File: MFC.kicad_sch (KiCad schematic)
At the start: 25 parts, among them J1 DB15_Female_MountingHoles, J10 Conn_01x01_Male, J11 Conn_01x01_Male, J12 Conn_01x01_Male, J2 Conn_01x04_Male, J4 647676-3, J5 Conn_01x01_Male, J6 Conn_01x01_Male

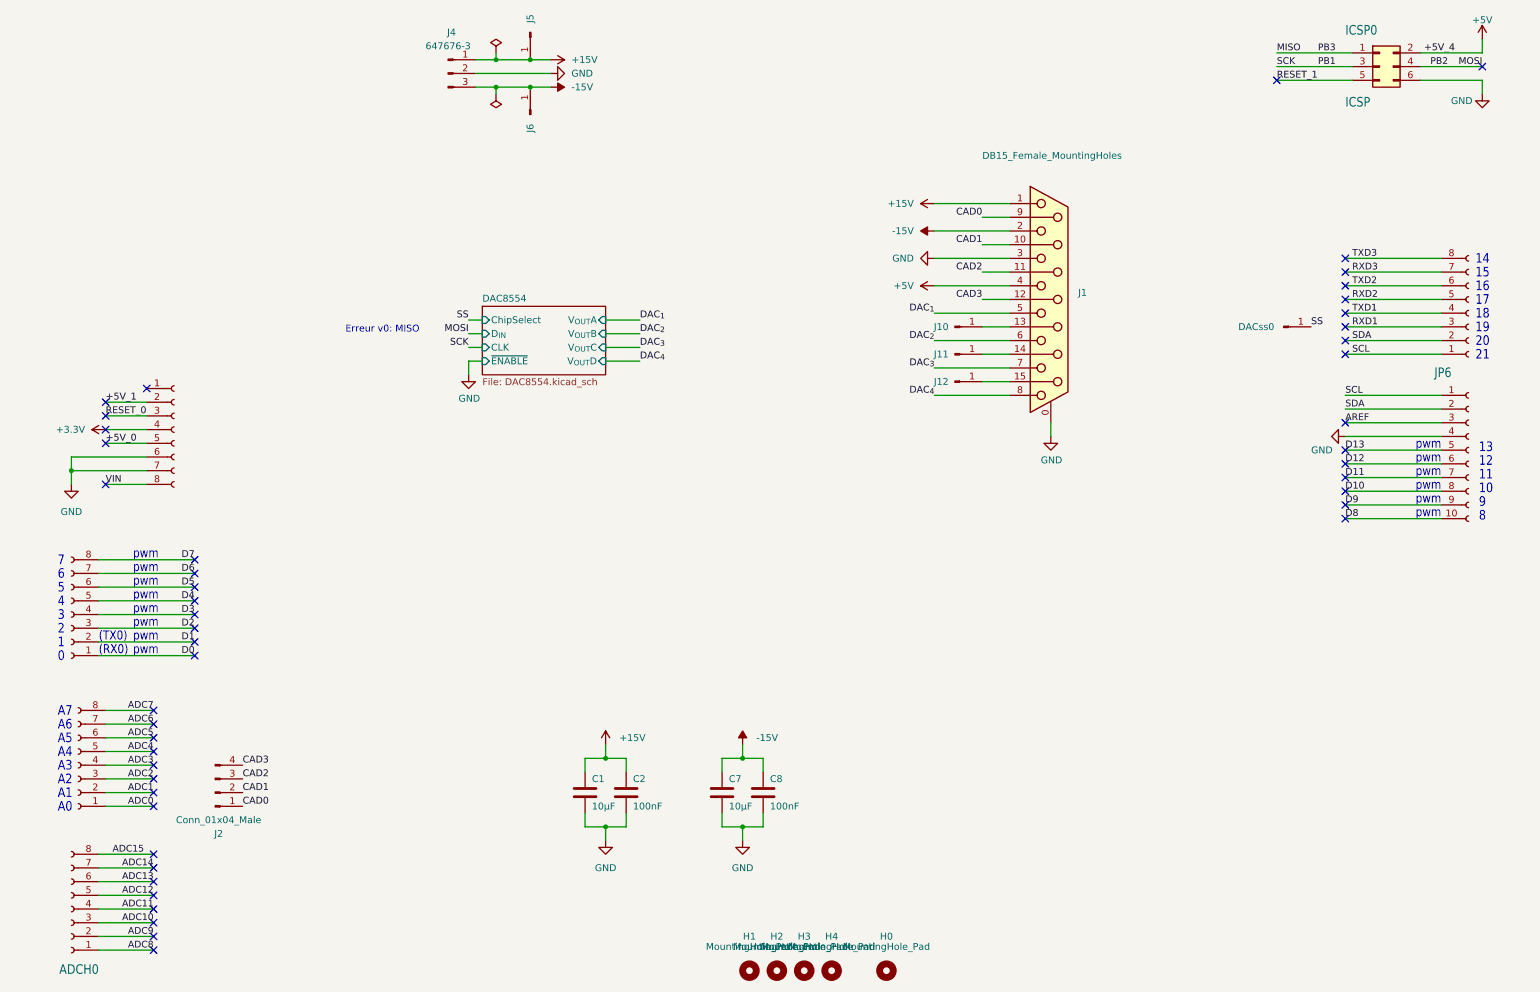
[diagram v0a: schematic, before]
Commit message: Update to KiCad 7
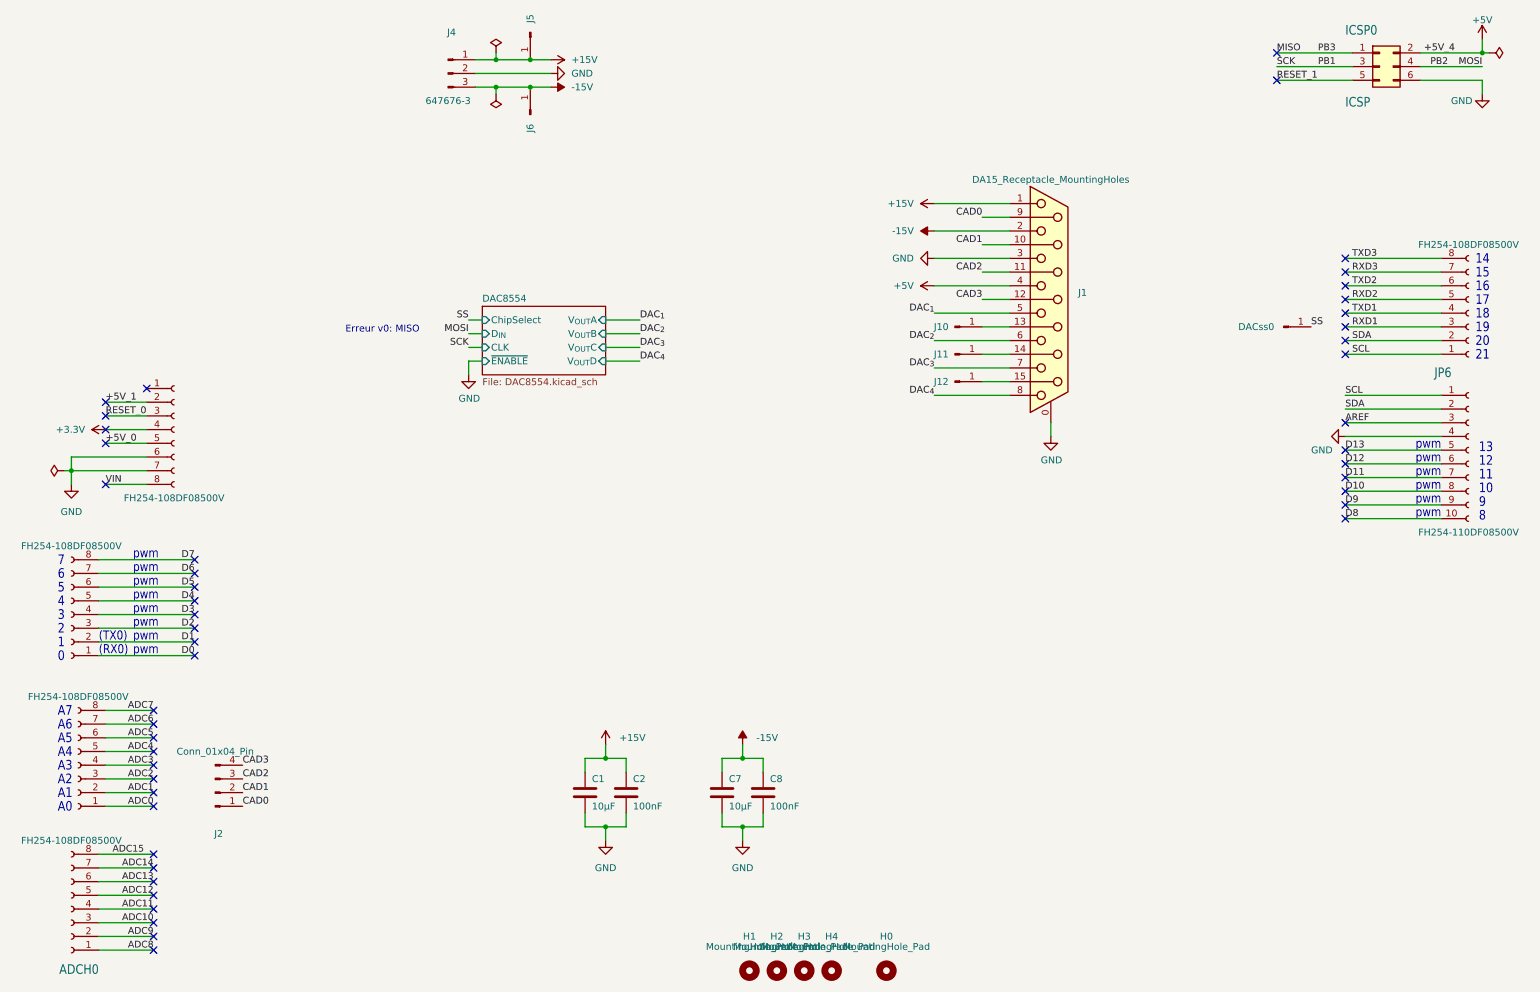
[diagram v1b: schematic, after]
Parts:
- ADCH0, ADCL0, COMMUNICATION0, POWER0, PWML0: symbol Connector:Conn_01x08_Female -> Connector:Conn_01x08_Socket
- DACss0, J10, J11, J12, J5, J6: value Conn_01x01_Male -> Conn_01x01_Pin; symbol Connector:Conn_01x01_Male -> Connector:Conn_01x01_Pin
- J1: value DB15_Female_MountingHoles -> DA15_Receptacle_MountingHoles; symbol Connector:DB15_Female_MountingHoles -> Connector:DA15_Receptacle_MountingHoles
- J2: value Conn_01x04_Male -> Conn_01x04_Pin; symbol Connector:Conn_01x04_Male -> Connector:Conn_01x04_Pin
- J4: symbol Connector:Conn_01x03_Male -> Connector:Conn_01x03_Pin
- JP6: symbol Connector:Conn_01x10_Female -> Connector:Conn_01x10_Socket

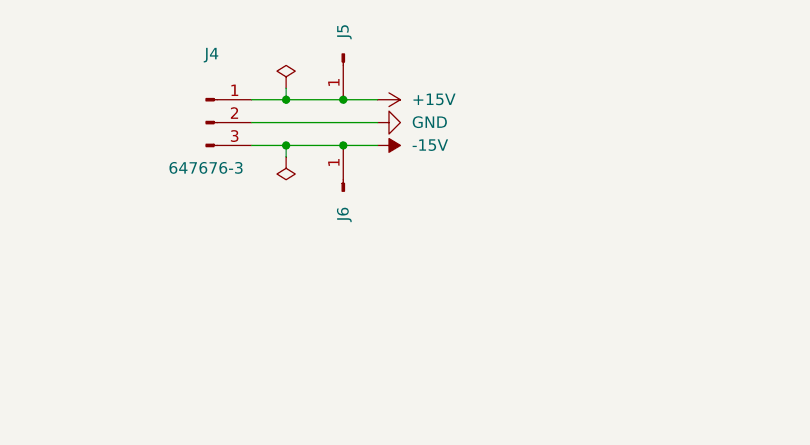
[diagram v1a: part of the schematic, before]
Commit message: Changed transversal power connector
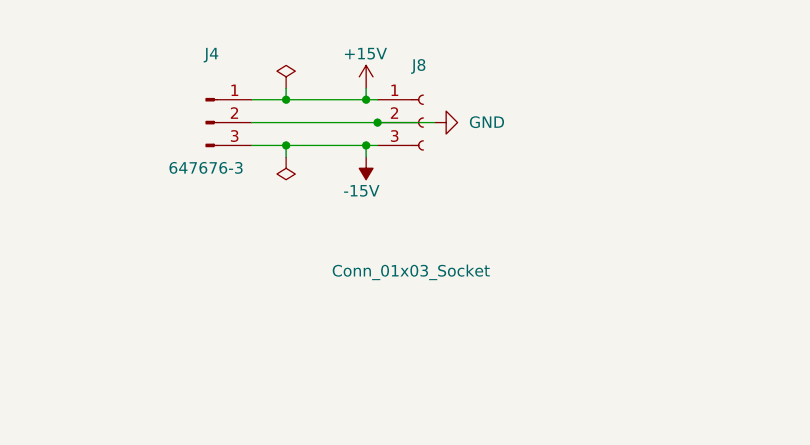
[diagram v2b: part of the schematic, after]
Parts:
- removed J5, J6: Conn_01x01_Pin, Connector_PinHeader_2.54mm:PinHeader_1x01_P2.54mm_Vertical, symbol Connector:Conn_01x01_Pin
- added J8: Conn_01x03_Socket, Connector_PinSocket_2.54mm:PinSocket_1x03_P2.54mm_Vertical, symbol Connector:Conn_01x03_Socket
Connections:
- net +15V: now also J8.1 (Pin_1)
- net -15V: now also J8.3 (Pin_3)
- net GND: now also J8.2 (Pin_2)

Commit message: Added MAX232 Optimised DAC8554 Routing
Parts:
- removed J10, J11: Conn_01x01_Pin, Connector_PinHeader_2.54mm:PinHeader_1x01_P2.54mm_Vertical, symbol Connector:Conn_01x01_Pin
- added J5, J6: Conn_01x03_Pin, Connector_PinHeader_2.54mm:PinHeader_1x03_P2.54mm_Vertical, symbol Connector:Conn_01x03_Pin
- added R1, R3: 0, Resistor_SMD:R_0603_1608Metric_Pad0.98x0.95mm_HandSolder, symbol Device:R
- added R2, R4: R, Resistor_SMD:R_0603_1608Metric_Pad0.98x0.95mm_HandSolder, symbol Device:R
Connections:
- net GND: now also R2.2, R4.2
- net RXD2: now also J6.1 (Pin_1)
- net TXD2: now also J5.1 (Pin_1)
- net Serial_MISO: now reaches J1.14 (P14)
- net Serial_MISO: now also R3.2, R4.1
- net Serial_MOSI: now reaches J1.13 (P13)
- net Serial_MOSI: now also R1.2, R2.1
- new net: J6.2 (Pin_2), R3.1
- new net: J5.2 (Pin_2), R1.1
- new net RS232_MISO: J6.3 (Pin_3)
- new net RS232_MOSI: J5.3 (Pin_3)
- no-connect marks 47 -> 45
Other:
- added sheet MAX232 (MAX232.kicad_sch)
- moved on the sheet: C1, C2, C7, C8

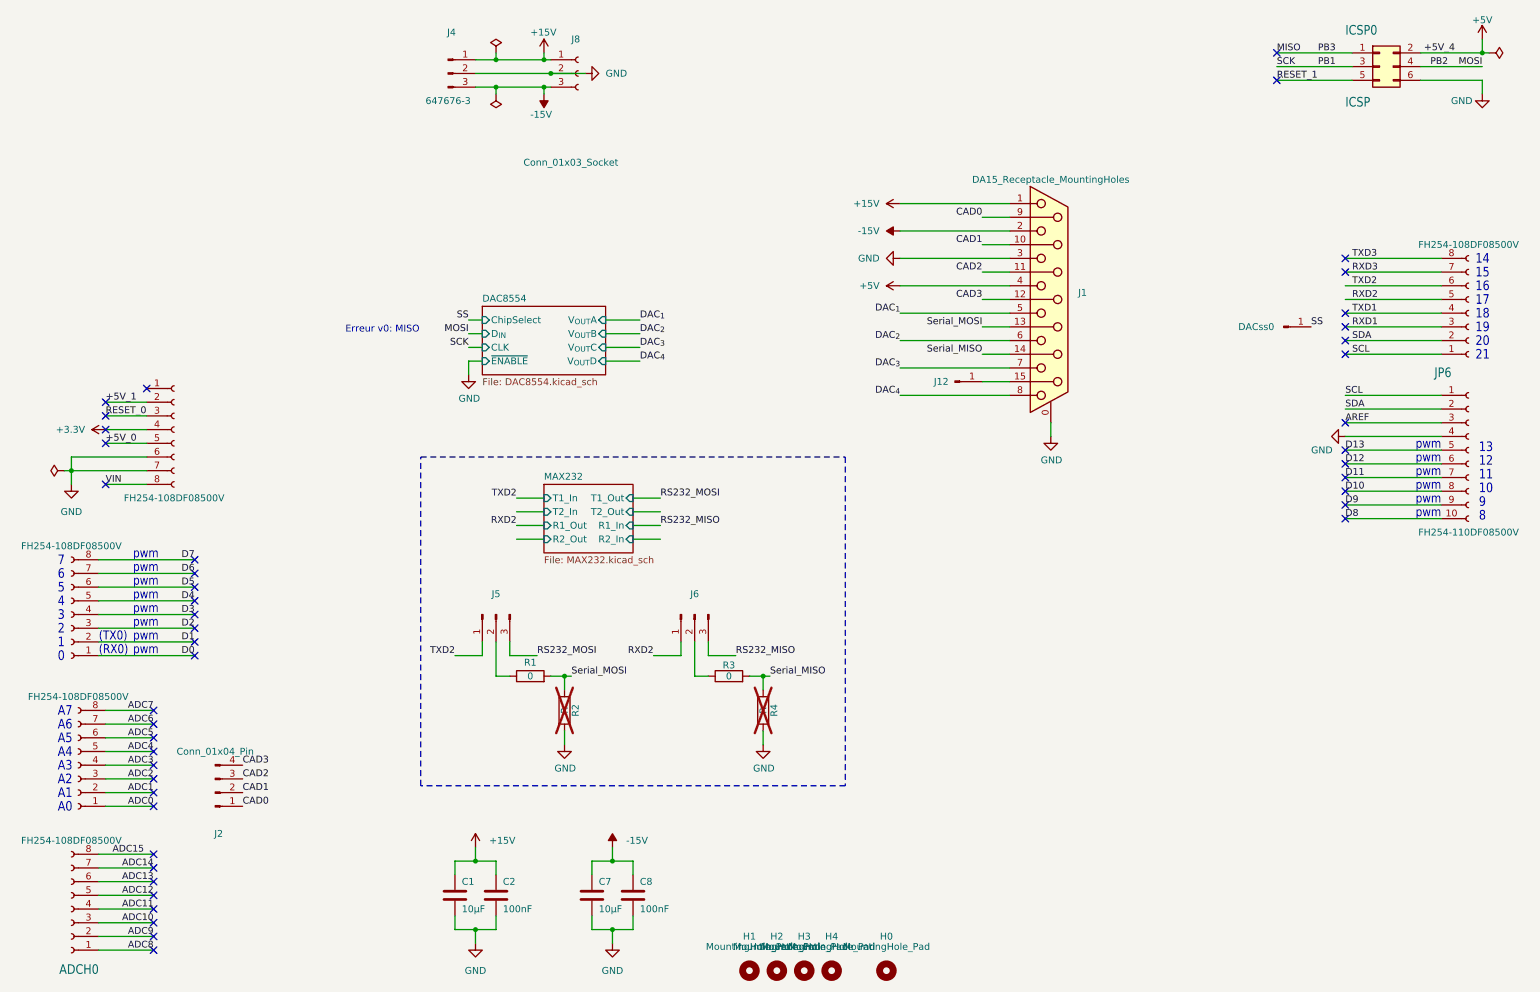
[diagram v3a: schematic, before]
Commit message: Added choice for serial com
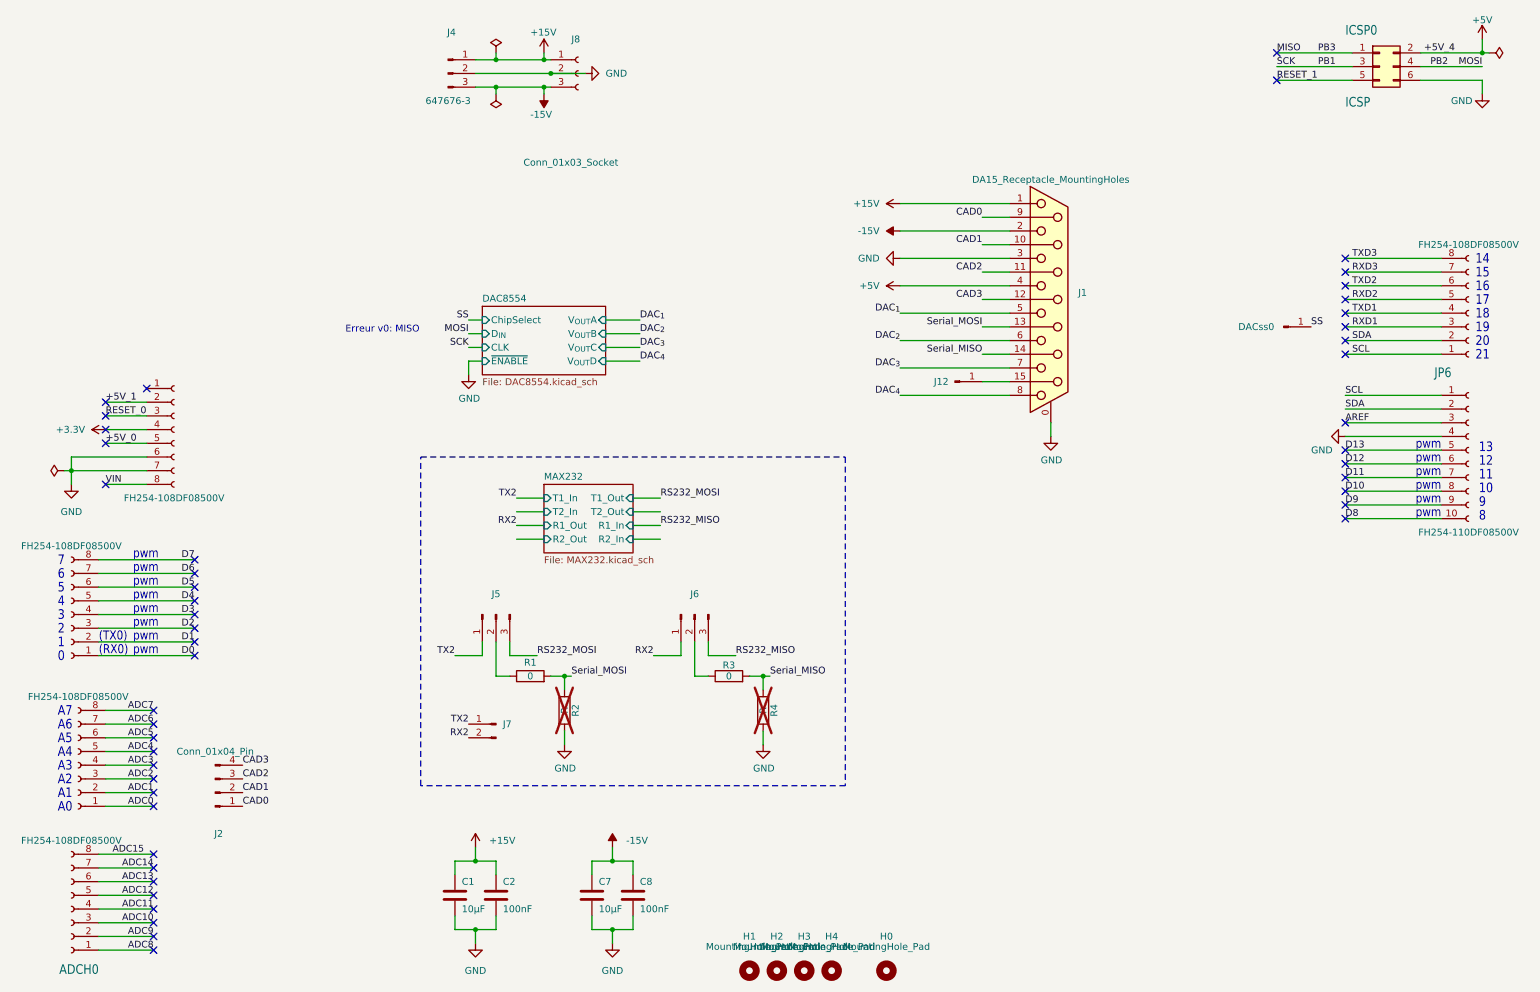
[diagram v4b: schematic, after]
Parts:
- added J7: Conn_01x02_Pin, Connector_PinHeader_2.54mm:PinHeader_1x02_P2.54mm_Vertical, symbol Connector:Conn_01x02_Pin
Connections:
- net RXD2: no longer J6.1 (Pin_1)
- net TXD2: no longer J5.1 (Pin_1)
- new net RX2: J6.1 (Pin_1), J7.2 (Pin_2)
- new net TX2: J5.1 (Pin_1), J7.1 (Pin_1)
- no-connect marks 45 -> 47
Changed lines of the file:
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@@
   (no_connect (at 31.75 176.53))
   (no_connect (at 22.86 102.87))
+  (no_connect (at 252.73 68.58))
   (no_connect (at 252.73 60.96))
   (no_connect (at 39.37 121.92))
@@
   (no_connect (at 31.75 189.23))
   (no_connect (at 31.75 181.61))
+  (no_connect (at 252.73 66.04))
   (no_connect (at 31.75 152.4))
   (no_connect (at 30.48 85.09))
@@
     (effects (font (size 1.27 1.27)) (justify right bottom))
   )
-  (label "RXD2" (at 124.46 134.62 180) (fields_autoplaced)
+  (label "RX2" (at 124.46 134.62 180) (fields_autoplaced)
     (effects (font (size 1.2446 1.2446)) (justify right bottom))
   )
@@
     (effects (font (size 1.27 1.27)) (justify left bottom))
   )
-  (label "TXD2" (at 99.06 105.41 180) (fields_autoplaced)
+  (label "TX2" (at 99.06 105.41 180) (fields_autoplaced)
     (effects (font (size 1.2446 1.2446)) (justify right bottom))
   )
@@
     (effects (font (size 1.27 1.27)) (justify left bottom))
   )
+  (label "TX2" (at 90.17 147.32 180) (fields_autoplaced)
+    (effects (font (size 1.2446 1.2446)) (justify right bottom))
+  )
   (label "D8" (at 252.73 109.22 0) (fields_autoplaced)
     (effects (font (size 1.27 1.27)) (justify left bottom))
@@
     (effects (font (size 1.2446 1.2446)) (justify left bottom))
   )
-  (label "TXD2" (at 87.63 134.62 180) (fields_autoplaced)
-    (effects (font (size 1.2446 1.2446)) (justify right bottom))
-  )
-  (label "RXD2" (at 99.06 110.49 180) (fields_autoplaced)
+  (label "TX2" (at 87.63 134.62 180) (fields_autoplaced)
+    (effects (font (size 1.2446 1.2446)) (justify right bottom))
+  )
+  (label "RX2" (at 90.17 149.86 180) (fields_autoplaced)
+    (effects (font (size 1.2446 1.2446)) (justify right bottom))
+  )
+  (label "RX2" (at 99.06 110.49 180) (fields_autoplaced)
     (effects (font (size 1.2446 1.2446)) (justify right bottom))
   )
@@
         )
       )
+    )
+  )
+  (symbol (lib_id "Connector:Conn_01x02_Pin") (at 95.25 147.32 0) (mirror y) (unit 1)
+    (in_bom yes) (on_board yes) (dnp no) (fields_autoplaced)
+    (property "Reference" "J7" (at 96.52 147.32 0)
+      (effects (font (size 1.27 1.27)) (justify right))
+    )
+    (property "Value" "Conn_01x02_Pin" (at 96.52 149.86 0)
+      (effects (font (size 1.27 1.27)) (justify right) hide)
+    )
+    (property "Footprint" "Connector_PinHeader_2.54mm:PinHeader_1x02_P2.54mm_Vertical" (at 95.25 147.32 0)
+      (effects (font (size 1.27 1.27)) hide)
+    )
+    (property "Datasheet" "~" (at 95.25 147.32 0)
+      (effects (font (size 1.27 1.27)) hide)
+    )
+    (pin "1")
+    (pin "2")
+    (instances
+      (project "MFC"
+        (path "/b2d5fb00-0584-4253-bf32-ef41fb78b640"
+          (reference "J7") (unit 1)
+        )
+      )

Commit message: Update 10u capa for tantal
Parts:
- C1, C7: footprint Capacitor_SMD:C_0603_1608Metric_Pad1.08x0.95mm_HandSolder -> Capacitor_SMD:C_1206_3216Metric_Pad1.33x1.80mm_HandSolder
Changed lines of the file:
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@@
       (effects (font (size 1.27 1.27)) (justify left))
     )
-    (property "Footprint" "Capacitor_SMD:C_0603_1608Metric_Pad1.08x0.95mm_HandSolder" (at 113.9952 182.88 0)
+    (property "Footprint" "Capacitor_SMD:C_1206_3216Metric_Pad1.33x1.80mm_HandSolder" (at 113.9952 182.88 0)
       (effects (font (size 1.27 1.27)) hide)
     )
@@
       (effects (font (size 1.27 1.27)) (justify left))
     )
-    (property "Footprint" "Capacitor_SMD:C_0603_1608Metric_Pad1.08x0.95mm_HandSolder" (at 88.5952 182.88 0)
-      (effects (font (size 1.27 1.27)) hide)
-    )
+    (property "Footprint" "Capacitor_SMD:C_1206_3216Metric_Pad1.33x1.80mm_HandSolder" (at 88.5952 182.88 0)
+      (effects (font (size 1.27 1.27)) hide)
+    )
